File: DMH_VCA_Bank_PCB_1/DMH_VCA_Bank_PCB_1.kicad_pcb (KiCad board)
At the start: 2 copper layers, 48 x 175 mm, 111 parts, among them J1 TS_Jack_6.35mm_Sw, J10 TS_Jack_6.35mm_Sw, J100 IDC_02x05, J11 TS_Jack_6.35mm_Sw, J12 TS_Jack_6.35mm_Sw, J2 TS_Jack_6.35mm_Sw, J200 IDC_02x08, J3 TS_Jack_6.35mm_Sw, J4 TS_Jack_6.35mm_Sw, J5 TS_Jack_6.35mm_Sw, J50 Conn_01x06, J6 TS_Jack_6.35mm_Sw, J60 Conn_01x06, J7 TS_Jack_6.35mm_Sw, J70 Conn_01x06, J8 TS_Jack_6.35mm_Sw, J80 Conn_01x06, J9 TS_Jack_6.35mm_Sw, Q1 BC548, Q2 BC548, Q3 BC548, Q4 BC548, Q5 BC548, Q6 BC548, Q7 BC548, Q8 BC548, U1 TL074, U2 TL074, U3 TL074

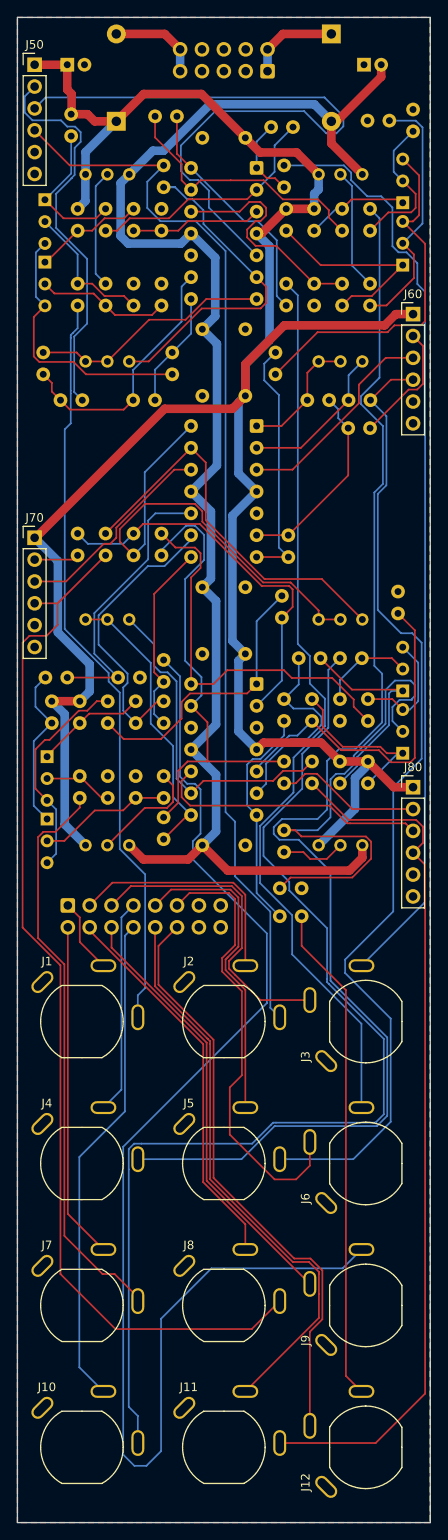
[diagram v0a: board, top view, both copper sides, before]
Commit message: All PCB 1 errors solved
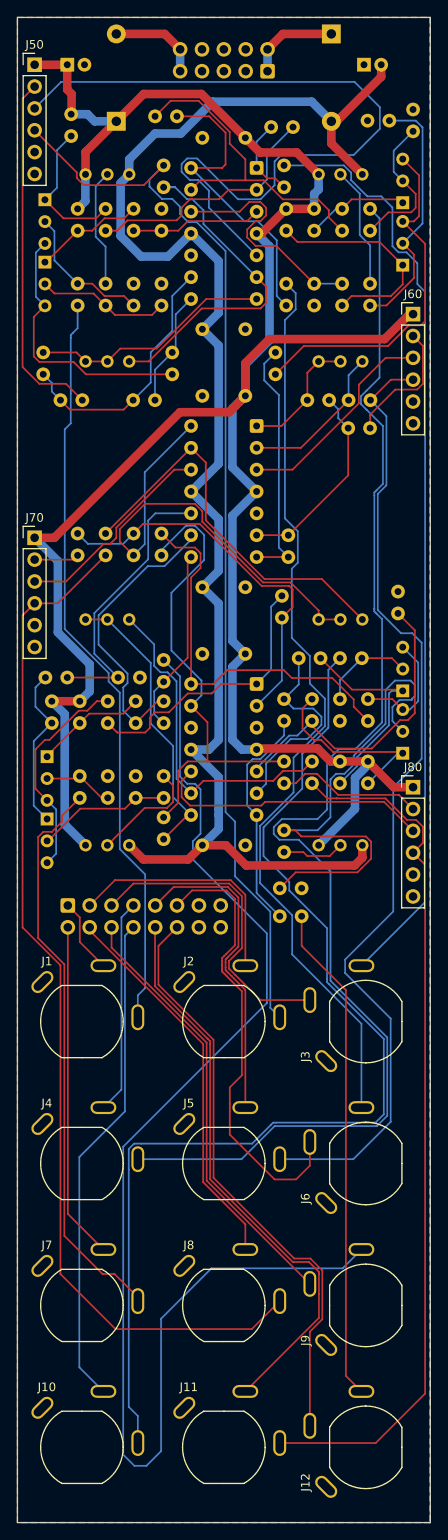
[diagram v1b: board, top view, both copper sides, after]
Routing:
- net /Inputs and Outputs/CV Amt A Pot: track 77.5 -> 90.2 mm
- net Net-(R18-Pad1): track 28.2 -> 35.8 mm
- net Net-(U1D--): track 31.2 -> 38.2 mm
- net -12V: track 173.1 -> 178.0 mm
- net /Inputs and Outputs/Offset A Pot: track 45.8 -> 41.7 mm
- net Net-(U3B-+): track 40.8 -> 36.8 mm
- net Net-(Q8-C): track 19.8 -> 22.2 mm
- net /Inputs and Outputs/CV C Jack: track 122.7 -> 120.4 mm
- net +12V: track 267.7 -> 269.3 mm
- net /Inputs and Outputs/Output B Jack: track 105.7 -> 107.3 mm
- net Net-(U3D--): track 55.4 -> 56.7 mm
- net Net-(Q4-C): track 24.2 -> 25.5 mm
- net Net-(R32-Pad2): track 33.3 -> 32.3 mm
- net /Inputs and Outputs/CV A Jack: track 125.3 -> 126.3 mm
- net Net-(R44-Pad1): track 22.5 -> 21.6 mm
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
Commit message: PCB 1 Optimized
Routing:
- net Net-(U2C--): track 33.9 -> 44.9 mm
- net Net-(U3D--): track 56.7 -> 46.6 mm
- net Net-(U2C-+): track 33.2 -> 39.3 mm
- net /Inputs and Outputs/CV B Jack: track 114.5 -> 117.5 mm
- net /Inputs and Outputs/Output D Jack: track 58.1 -> 60.8 mm
- net Net-(Q8-B): track 60.6 -> 58.5 mm
- net /Inputs and Outputs/CV D Jack: track 101.2 -> 102.9 mm
- net Net-(Q1-E): track 31.5 -> 32.5 mm
- net /Inputs and Outputs/Output C Jack: track 153.2 -> 154.2 mm
- net /Inputs and Outputs/CV Amt A Pot: track 90.2 -> 91.2 mm
- net Net-(J200-Pin_12): track 57.7 -> 58.6 mm
- net Net-(R18-Pad1): track 35.8 -> 35.0 mm
- net /Inputs and Outputs/Output A Jack: track 108.5 -> 109.1 mm
- net -12V: track 178.0 -> 177.5 mm

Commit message: Generated Gerbers
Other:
- board text added: "Mk1.0 - October 2025"
- board text removed: "Mk1.0 - Month 2025"
